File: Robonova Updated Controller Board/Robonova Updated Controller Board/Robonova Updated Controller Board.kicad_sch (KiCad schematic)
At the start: 75 parts

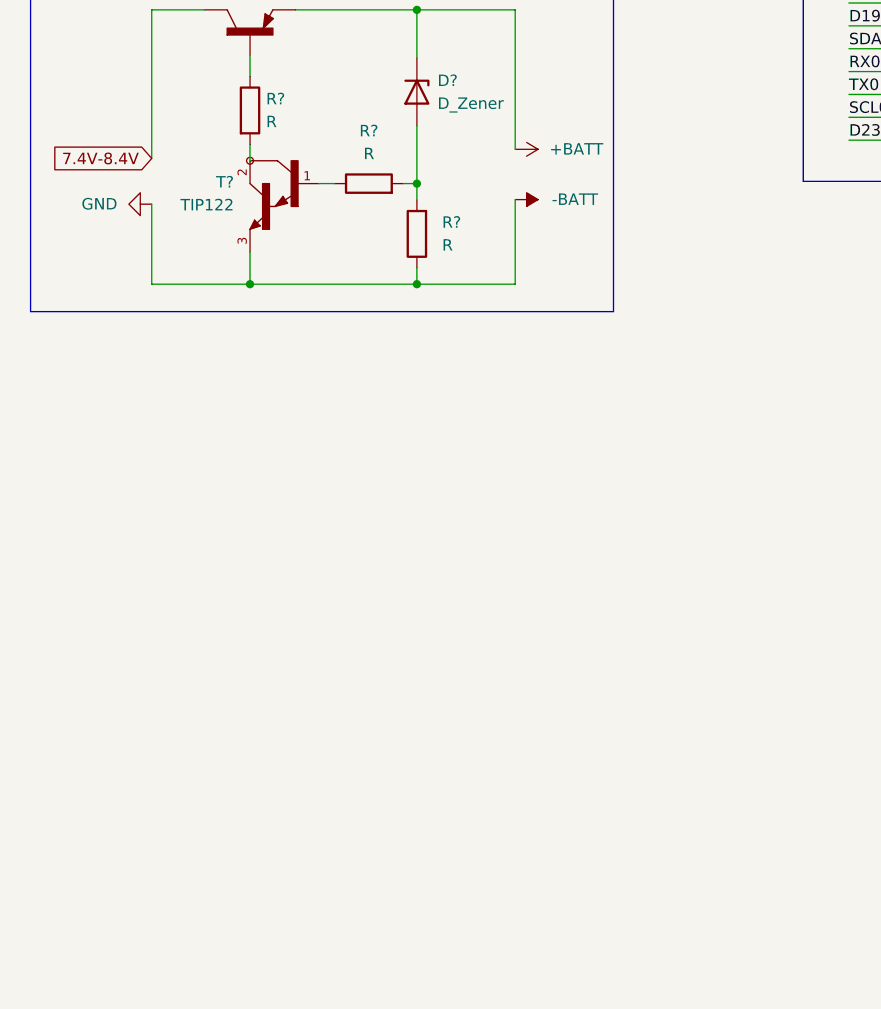
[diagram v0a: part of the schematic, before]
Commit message: started usb-C power connector schematic
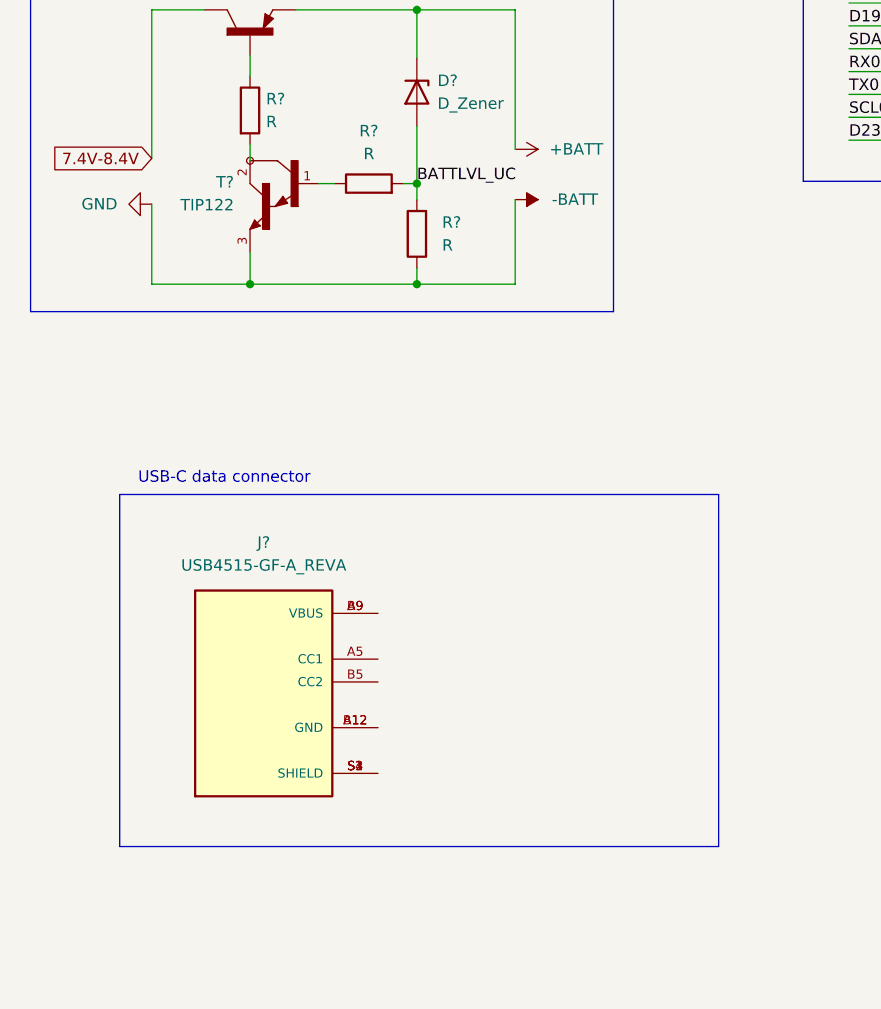
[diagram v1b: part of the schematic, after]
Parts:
- added J?: USB4515-GF-A_REVA, GCT_USB4515-GF-A_REVA, symbol USB4515-GF-A_REVA:USB4515-GF-A_REVA
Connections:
- net BATTLVL_UC: now reaches D?.2 (A), R?.2, R?.2
- new net: J?.A12 (GND), J?.B12 (GND)
- new net: J?.A9 (VBUS), J?.B9 (VBUS)
- new net: J?.S1 (SHIELD), J?.S2 (SHIELD), J?.S3 (SHIELD), J?.S4 (SHIELD)
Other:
- note added: "USB-C data connector"
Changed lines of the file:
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@@
     (stroke (width 0) (type default) (color 0 0 0 0))
   )
+  (polyline (pts (xy 28.448 149.606) (xy 28.448 188.722))
+    (stroke (width 0) (type default) (color 0 0 0 0))
+  )
   (wire (pts (xy 466.09 115.824) (xy 473.71 115.824))
     (stroke (width 0) (type default) (color 0 0 0 0))
@@
     (stroke (width 0) (type default) (color 0 0 0 0))
   )
+  (polyline (pts (xy 94.996 188.722) (xy 28.448 188.722))
+    (stroke (width 0) (type default) (color 0 0 0 0))
+  )
   (wire (pts (xy 61.468 108.712) (xy 61.468 115.062))
     (stroke (width 0) (type default) (color 0 0 0 0))
@@
     (stroke (width 0) (type default) (color 0 0 0 0))
   )
+  (polyline (pts (xy 28.448 149.606) (xy 94.996 149.606))
+    (stroke (width 0) (type default) (color 0 0 0 0))
+  )
   (wire (pts (xy 397.764 115.062) (xy 397.764 92.202))
     (stroke (width 0) (type default) (color 0 0 0 0))
@@
     (stroke (width 0) (type default) (color 0 0 0 0))
   )
+  (polyline (pts (xy 94.996 149.606) (xy 94.996 188.722))
+    (stroke (width 0) (type default) (color 0 0 0 0))
+  )
   (wire (pts (xy 428.498 210.058) (xy 420.878 210.058))
     (stroke (width 0) (type default) (color 0 0 0 0))
@@
     (effects (font (size 1.4986 1.4986)) (justify left bottom))
   )
+  (text "USB-C data connector\n" (at 30.48 148.59 0)
+    (effects (font (size 1.27 1.27)) (justify left bottom))
+  )
   (text "VIN 1.8V to 5.5V" (at 414.02 283.972 180)
     (effects (font (size 1.778 1.778)) (justify left bottom))
@@
     (effects (font (size 1.27 1.27)) (justify left bottom))
   )
+  (label "BATTLVL_UC" (at 61.468 115.062 0)
+    (effects (font (size 1.27 1.27)) (justify left bottom))
+  )
   (label "D19" (at 123.19 61.976 270)
     (effects (font (size 1.27 1.27)) (justify right bottom))
@@
     (pin "1")
   )
+  (symbol (lib_id "USB4515-GF-A_REVA:USB4515-GF-A_REVA") (at 44.45 170.434 0) (unit 1)
+    (in_bom yes) (on_board yes) (fields_autoplaced)
+    (property "Reference" "J?" (id 0) (at 44.45 154.94 0))
+    (property "Value" "USB4515-GF-A_REVA" (id 1) (at 44.45 157.48 0))
+    (property "Footprint" "GCT_USB4515-GF-A_REVA" (id 2) (at 44.45 170.434 0)
+      (effects (font (size 1.27 1.27)) (justify left bottom) hide)
+    )
+    (property "Datasheet" "" (id 3) (at 44.45 170.434 0)
+      (effects (font (size 1.27 1.27)) (justify left bottom) hide)
+    )
+    (property "MANUFACTURER" "GCT" (id 4) (at 44.45 170.434 0)
+      (effects (font (size 1.27 1.27)) (justify left bottom) hide)
+    )
+    (property "STANDARD" "Manufacturer Recommendations" (id 5) (at 44.45 170.434 0)
+      (effects (font (size 1.27 1.27)) (justify left bottom) hide)
+    )
+    (property "PARTREV" "A" (id 6) (at 44.45 170.434 0)
+      (effects (font (size 1.27 1.27)) (justify left bottom) hide)
+    )
+    (property "MAXIMUM_PACKAGE_HEIGHT" "3.16 mm" (id 7) (at 44.45 170.434 0)
+      (effects (font (size 1.27 1.27)) (justify left bottom) hide)
+    )
+    (pin "A12")
+    (pin "A5")
+    (pin "A9")
+    (pin "B12")
+    (pin "B5")
+    (pin "B9")
+    (pin "S1")
+    (pin "S2")
+    (pin "S3")
+    (pin "S4")
+  )
   (symbol (lib_id "Adafruit-PCA9685-rev-C-rescue:GND-Adafruit_PCA9685_rev_C-eagle-import") (at 473.71 133.604 0) (mirror y) (unit 1)
     (in_bom yes) (on_board yes)
@@
       (reference "D?") (unit 1) (value "RED") (footprint "Robonova Updated Controller Board:LED-0603")
     )
+    (path "/a323fd43-1df3-4377-85b3-4b86fccd1c0c"
+      (reference "J?") (unit 1) (value "USB4515-GF-A_REVA") (footprint "GCT_USB4515-GF-A_REVA")
+    )
     (path "/ff48056d-c69c-4608-85c2-dc51fc757704"

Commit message: changed usb-c connector, started on mcu power regulator and cleaned up
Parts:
- removed C? (x2): 0.1uF, Robonova Updated Controller Board:0603, symbol Robonova Updated Controller Board-eagle-import:0.1UF-0603-25V-5%
- removed C? (x2): 1.0uF, Robonova Updated Controller Board:0603, symbol Robonova Updated Controller Board-eagle-import:1.0UF-0603-16V-10%-X7R
- removed C?: 10uF, Adafruit PCA9685 rev C:0805-NO, symbol Adafruit-PCA9685-rev-C-rescue:CAP_CERAMIC0805-NOOUTLINE-Adafruit_PCA9685_rev_C-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
- removed C?: CPOL-USE3.5-8, Adafruit PCA9685 rev C:E3,5-8, symbol Adafruit-PCA9685-rev-C-rescue:CPOL-USE3.5-8-Adafruit_PCA9685_rev_C-eagle-import
- removed D?: RED, Robonova Updated Controller Board:LED-0603, symbol Robonova Updated Controller Board-eagle-import:LED-RED0603
- removed J?: USB4515-GF-A_REVA, GCT_USB4515-GF-A_REVA, symbol USB4515-GF-A_REVA:USB4515-GF-A_REVA
- removed J?: TERMBLOCK_1X2, Adafruit PCA9685 rev C:TERMBLOCK_1X2-3.5MM, symbol Adafruit-PCA9685-rev-C-rescue:TERMBLOCK_1X2-Adafruit_PCA9685_rev_C-eagle-import
- removed JP? (x4): HEADER-3X04, Adafruit PCA9685 rev C:3X04, symbol Adafruit-PCA9685-rev-C-rescue:HEADER-3X04-Adafruit_PCA9685_rev_C-eagle-import
- removed JP? (x2): PINHD-1X6CB, Adafruit PCA9685 rev C:1X06-CLEANBIG, symbol Adafruit-PCA9685-rev-C-rescue:PINHD-1X6CB-Adafruit_PCA9685_rev_C-eagle-import
- removed JP?: AUX, Robonova Updated Controller Board:SMT-JUMPER_3_2-NC_TRACE_SILK, symbol Robonova Updated Controller Board-eagle-import:JUMPER-SMT_3_2-NC_TRACE_SILK
- removed JP?: LED, Robonova Updated Controller Board:SMT-JUMPER_2_NC_TRACE_SILK, symbol Robonova Updated Controller Board-eagle-import:JUMPER-SMT_2_NC_TRACE_SILK
- removed JP?: I2C PU, Robonova Updated Controller Board:SMT-JUMPER_3_2-NC_TRACE_SILK, symbol Robonova Updated Controller Board-eagle-import:JUMPER-SMT_3_2-NC_TRACE_SILK
- removed JP?: ADR, Robonova Updated Controller Board:SMT-JUMPER_2_NO_SILK, symbol Robonova Updated Controller Board-eagle-import:JUMPER-SMT_2_NO_SILK
- removed LED?: GREEN, Adafruit PCA9685 rev C:CHIPLED_0805_NOOUTLINE, symbol Adafruit-PCA9685-rev-C-rescue:LED0805_NOOUTLINE-Adafruit_PCA9685_rev_C-eagle-im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
- removed Q?: AOD417, Adafruit PCA9685 rev C:TO252, symbol Adafruit-PCA9685-rev-C-rescue:MOSFET-PTO252-Adafruit_PCA9685_rev_C-eagle-import
- removed Q? (x4): 20V/0.2A/8MHz/1.2Ω/1Vth, Robonova Updated Controller Board:SOT-416FL, symbol Robonova Updated Controller Board-eagle-import:MOSFET-NCH-RE1C002UN
- removed R? (x4): 10K, Adafruit PCA9685 rev C:RESPACK_4X0603, symbol Adafruit-PCA9685-rev-C-rescue:RESISTOR_4PACK-Adafruit_PCA9685_rev_C-eagle-import
- removed R?: 10K, Adafruit PCA9685 rev C:0805-NO, symbol Adafruit-PCA9685-rev-C-rescue:RESISTOR0805_NOOUTLINE-Adafruit_PCA9685_rev_C-eag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
- removed R? (x16): 220, Adafruit PCA9685 rev C:RESPACK_4X0603, symbol Adafruit-PCA9685-rev-C-rescue:RESISTOR_4PACK-Adafruit_PCA9685_rev_C-eagle-import
- removed R?: 220, Robonova Updated Controller Board:0603, symbol Robonova Updated Controller Board-eagle-import:220OHM-0603-1/10W-1%
- removed R? (x8): 2.2k, Robonova Updated Controller Board:0402-TIGHT, symbol Robonova Updated Controller Board-eagle-import:2.2KOHM-0402T-1/16W-1%
- removed R?: 470, Adafruit PCA9685 rev C:_0805MP, symbol Adafruit-PCA9685-rev-C-rescue:RESISTOR_0805MP-Adafruit_PCA9685_rev_C-eagle-impo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
- removed SJ_A? (x2): SOLDERJUMPERREFLOW_NOPASTE, Adafruit PCA9685 rev C:SOLDERJUMPER_REFLOW_NOPASTE, symbol Adafruit-PCA9685-rev-C-rescue:SOLDERJUMPERREFLOW_NOPASTE-Adafruit_PCA9685_rev_C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
- removed TP?: 1.8V, Robonova Updated Controller Board:PAD.03X.03, symbol Robonova Updated Controller Board-eagle-import:TEST-POINT3
- removed TP? (x2): TESTPOINTROUND1MM, Adafruit PCA9685 rev C:TESTPOINT_ROUND_1MM, symbol Adafruit-PCA9685-rev-C-rescue:TESTPOINTROUND1MM-Adafruit_PCA9685_rev_C-eagle-im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
- removed U?: PCA9685, Adafruit PCA9685 rev C:TSSOP28, symbol Adafruit-PCA9685-rev-C-rescue:PCA9685-Adafruit_PCA9685_rev_C-eagle-import
- removed U?: 9DoF IMU, Robonova Updated Controller Board:QFN24-3X3, symbol Robonova Updated Controller Board-eagle-import:ICM-20948
- removed U?: 1.8V/100mA, Robonova Updated Controller Board:SC70, symbol Robonova Updated Controller Board-eagle-import:V_REG_SP6214-1.8V
- added J?: USB_C_Receptacle_USB2.0, symbol Connector:USB_C_Receptacle_USB2.0
- added R? (x2): 5.11K, symbol Device:R
- added R?: 1M, symbol Device:R
- added U?: LF33CDT, TO228P972X240-3N, symbol LF33CDT:LF33CDT
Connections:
- net -BATT: now also J?.A1 (GND), J?.A12 (GND), J?.B1 (GND), J?.B12 (GND), R?.2, R?.2, R?.2
- net VIN renamed UCVIN
- net UCVIN: now also U?.3 (OUT)
- new net: J?.B5 (CC2), R?.1
- new net: J?.A5 (CC1), R?.1
- new net: J?.S1 (SHIELD), R?.1
- new net 5V: J?.A4 (VBUS), J?.A9 (VBUS), J?.B4 (VBUS), J?.B9 (VBUS)
- new net D+: J?.A6 (D+), J?.B6 (D+)
- new net D-: J?.A7 (D-), J?.B7 (D-)
- no-connect marks 4 -> 2
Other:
- added sheet 16-servo-controller (16servocontroller_sch.kicad_sch)
- added sheet IMU (IMU.kicad_sch)
- note added: "3.3V Powersupply"
- note added: "ESP32-wroom-1-dev-board connector header"
- note removed: "ADR -> I2C Address ------------------- open -> 0x69 closed -> 0x68 *Closing AD0 precludes SPI"
- note removed: "Adress selector"
- note removed: "Connectors and power led"
- note removed: "Cut to disable PWR LED"
- note removed: "I2C Address selector"
- note removed: "IMU"
- note removed: "Open = 0 / Closed = 1"
- note removed: "Output pins servo's"
- note removed: "PCA9685 controller"
- note removed: "Reverse voltage protection (not required?)"
- note removed: "Servo's"
- note removed: "VIN 1.8V to 5.5V"
- note removed: "adress = 1 + A1 +A0 + RW"
- note removed: "esp32 wroom 1 dev board connector"
- note removed: "level shifting and pull-up disconnects"
- note removed: "voltage regulator"
- moved on the sheet: JL?, JR?, JSensor?, LS?, Q?, R?

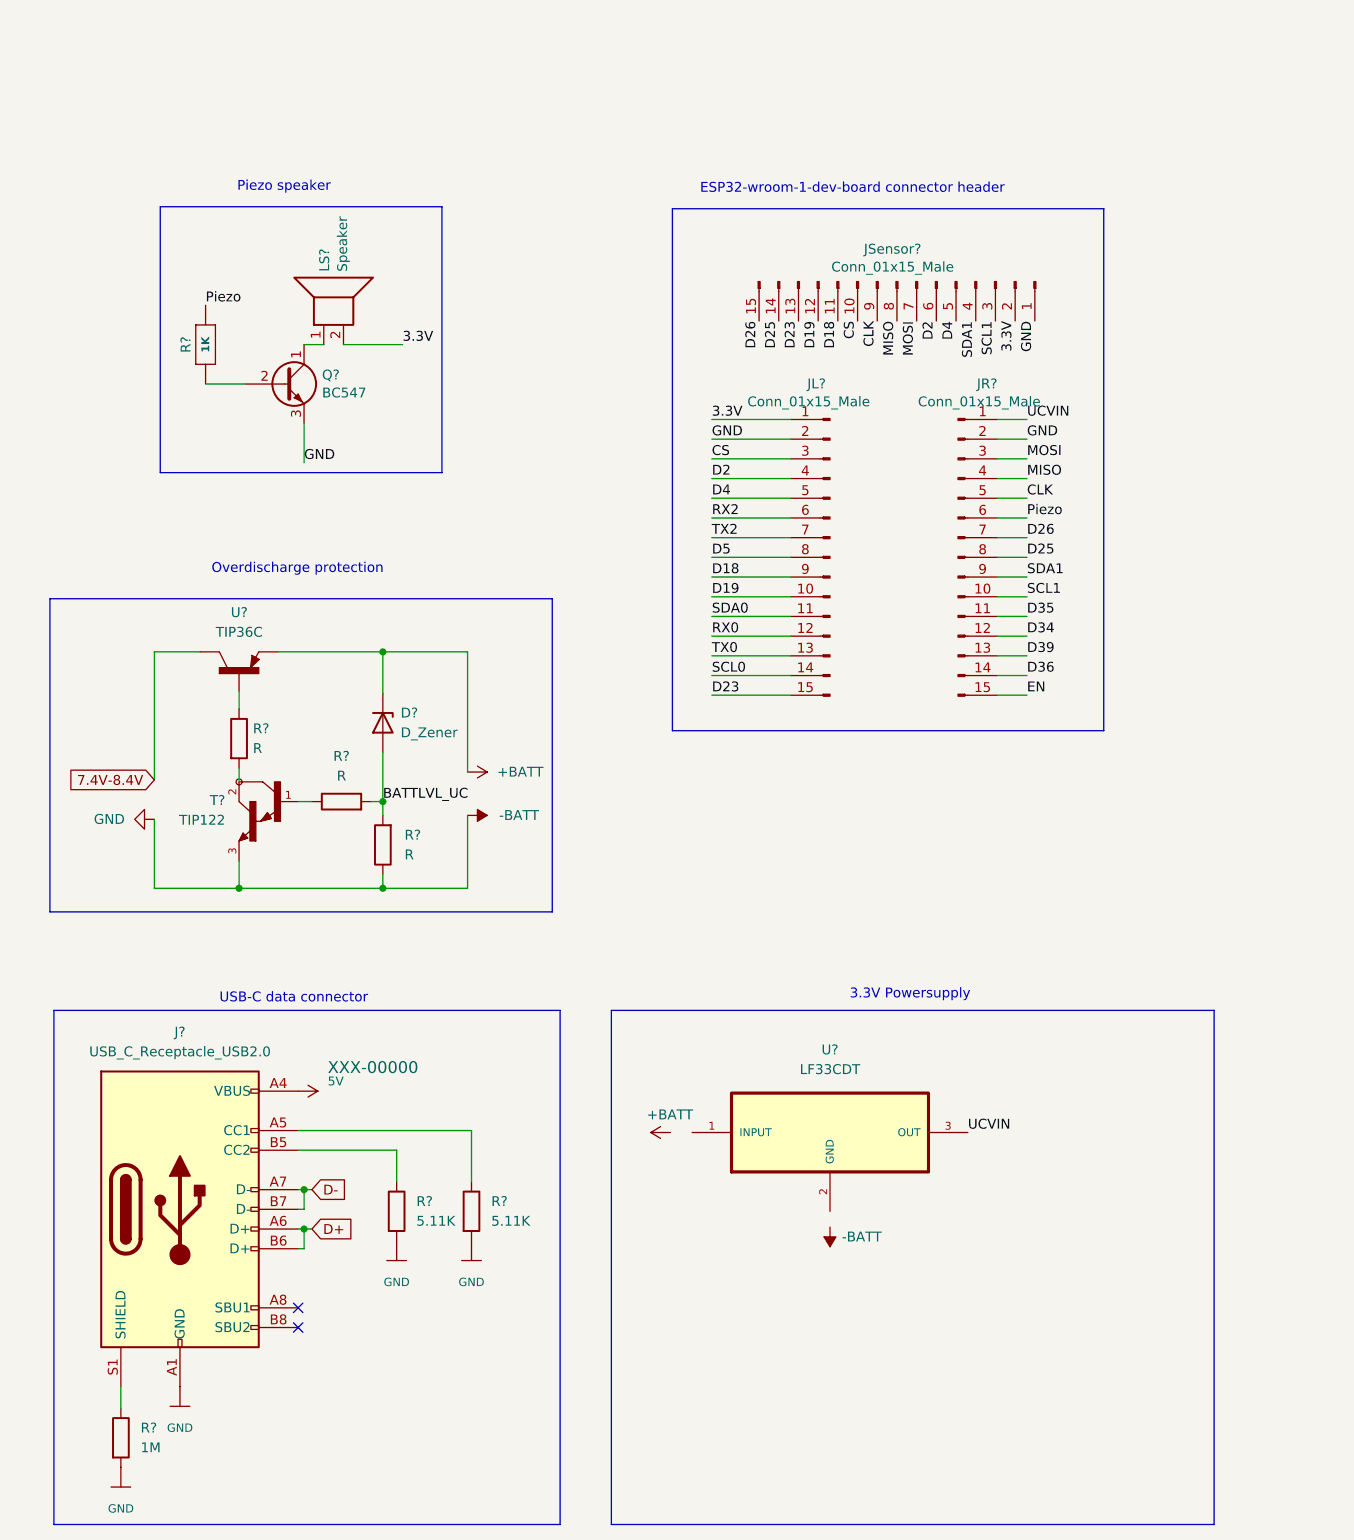
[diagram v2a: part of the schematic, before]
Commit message: Removed useless files and added some libraries to kicad
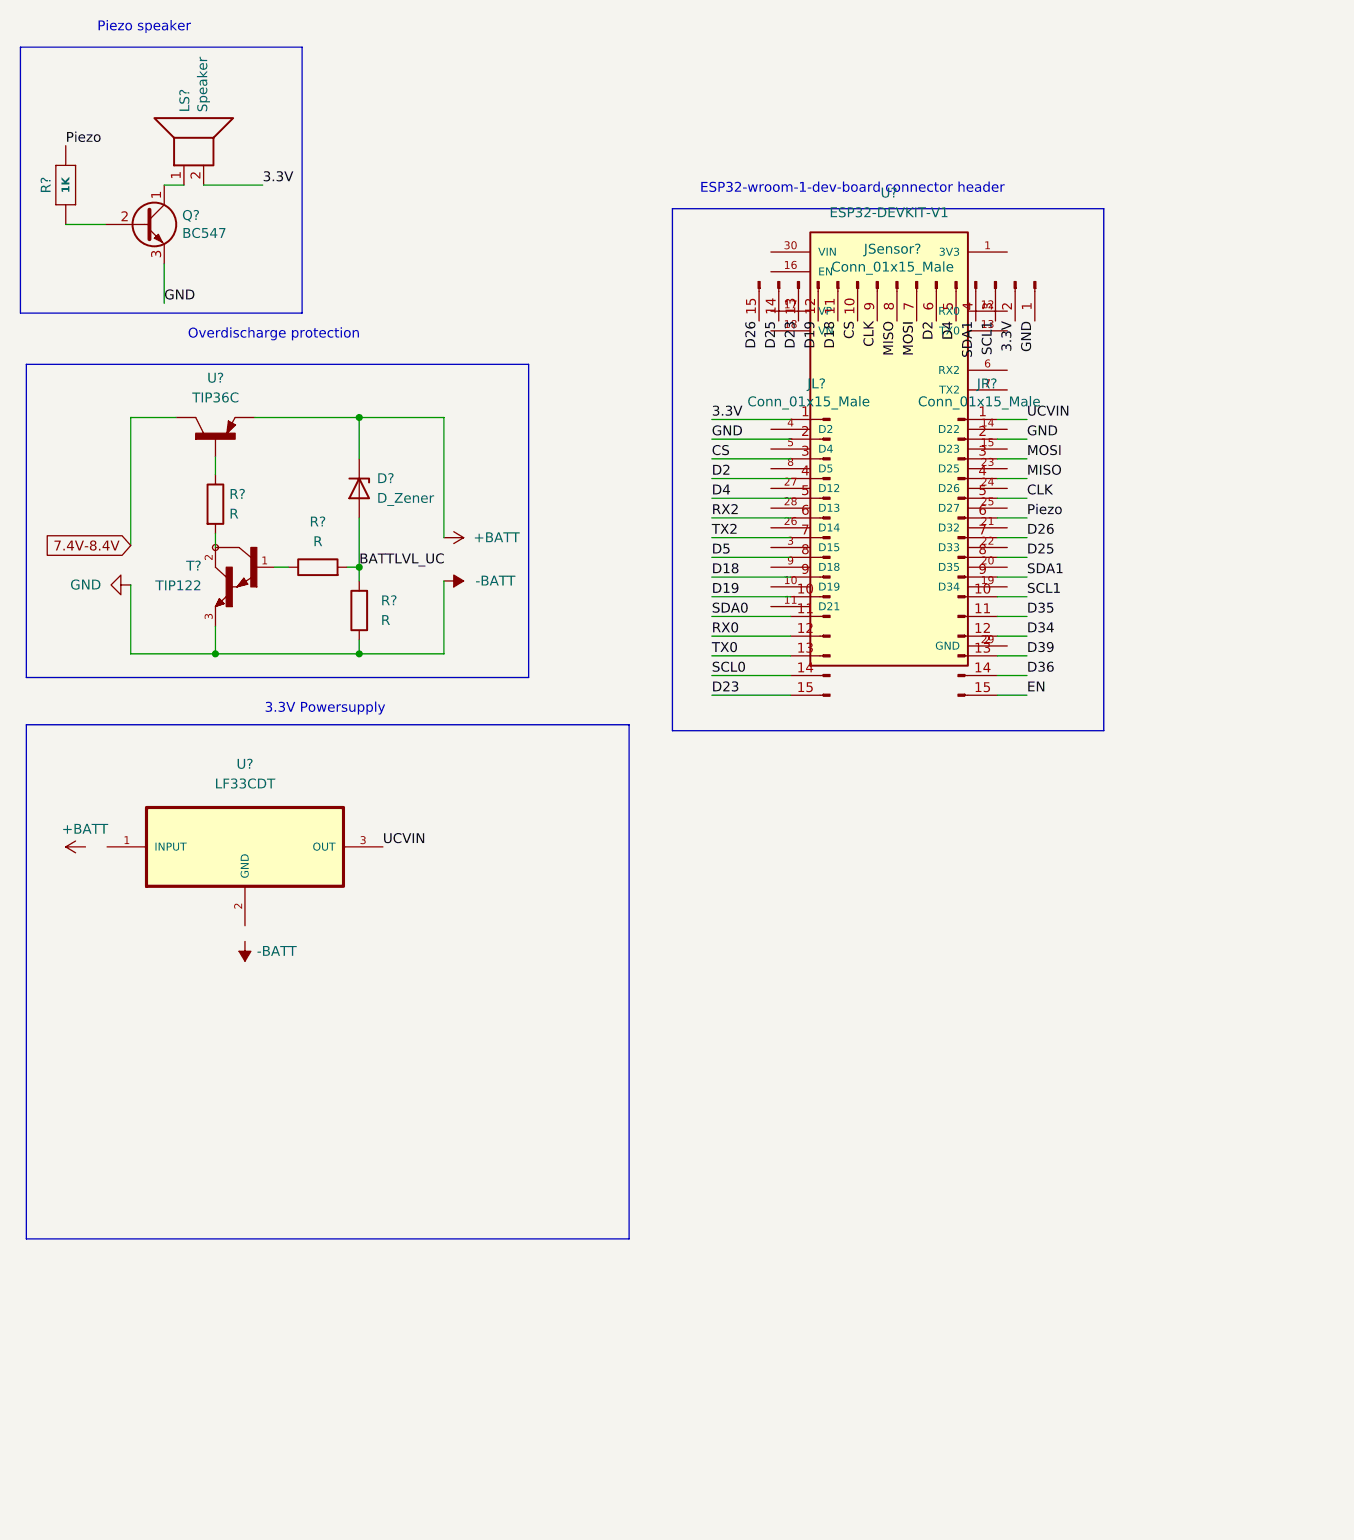
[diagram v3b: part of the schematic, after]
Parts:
- removed J?: USB_C_Receptacle_USB2.0, symbol Connector:USB_C_Receptacle_USB2.0
- removed R? (x2): 5.11K, symbol Device:R
- removed R?: 1M, symbol Device:R
- added U?: ESP32-DEVKIT-V1, MODULE_ESP32_DEVKIT_V1, symbol ESP32-DEVKIT-V1:ESP32-DEVKIT-V1
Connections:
- new net: U?.2 (GND), U?.29 (GND)
- no-connect marks 2 -> 0
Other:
- note removed: "USB-C data connector"
- moved on the sheet: D?, LS?, Q?, R?, T?, U?
